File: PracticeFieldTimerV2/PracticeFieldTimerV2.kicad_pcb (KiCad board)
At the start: 2 copper layers, 106 x 153.7 mm, 41 parts, among them J1 External Controls, J3 Panel, J5 /CAN Enable, J6 RJ45-B, J7 RJ45-A, J8 CAN Terminate, U1 ESP32-DevKitC, U2 PCF8574N, U3 20 x 4 LCD, U4 DS3231MZ_TRL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

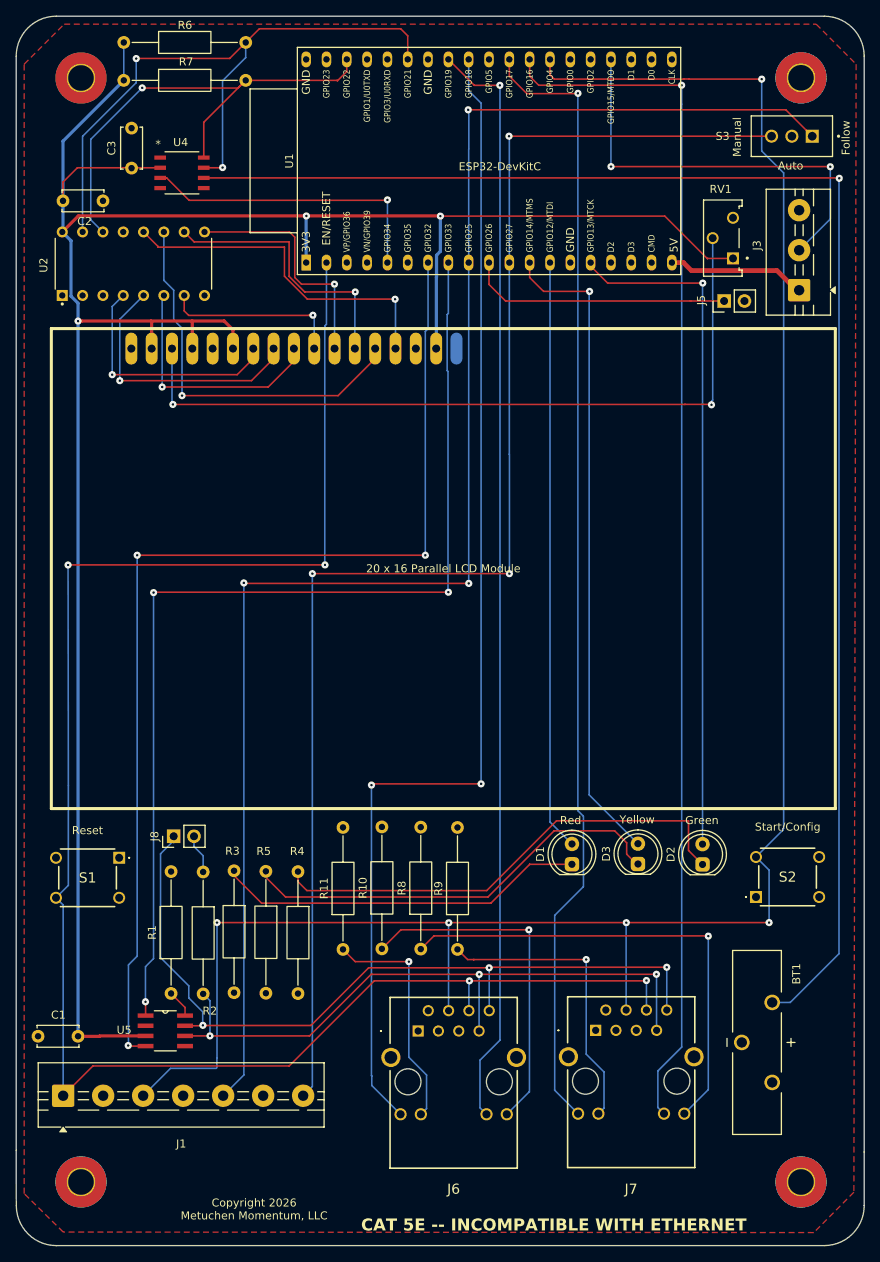
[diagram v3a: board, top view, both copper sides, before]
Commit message: Mark resistors with values. Add mounting holes for the LCD display. Needlessy tweak board width.
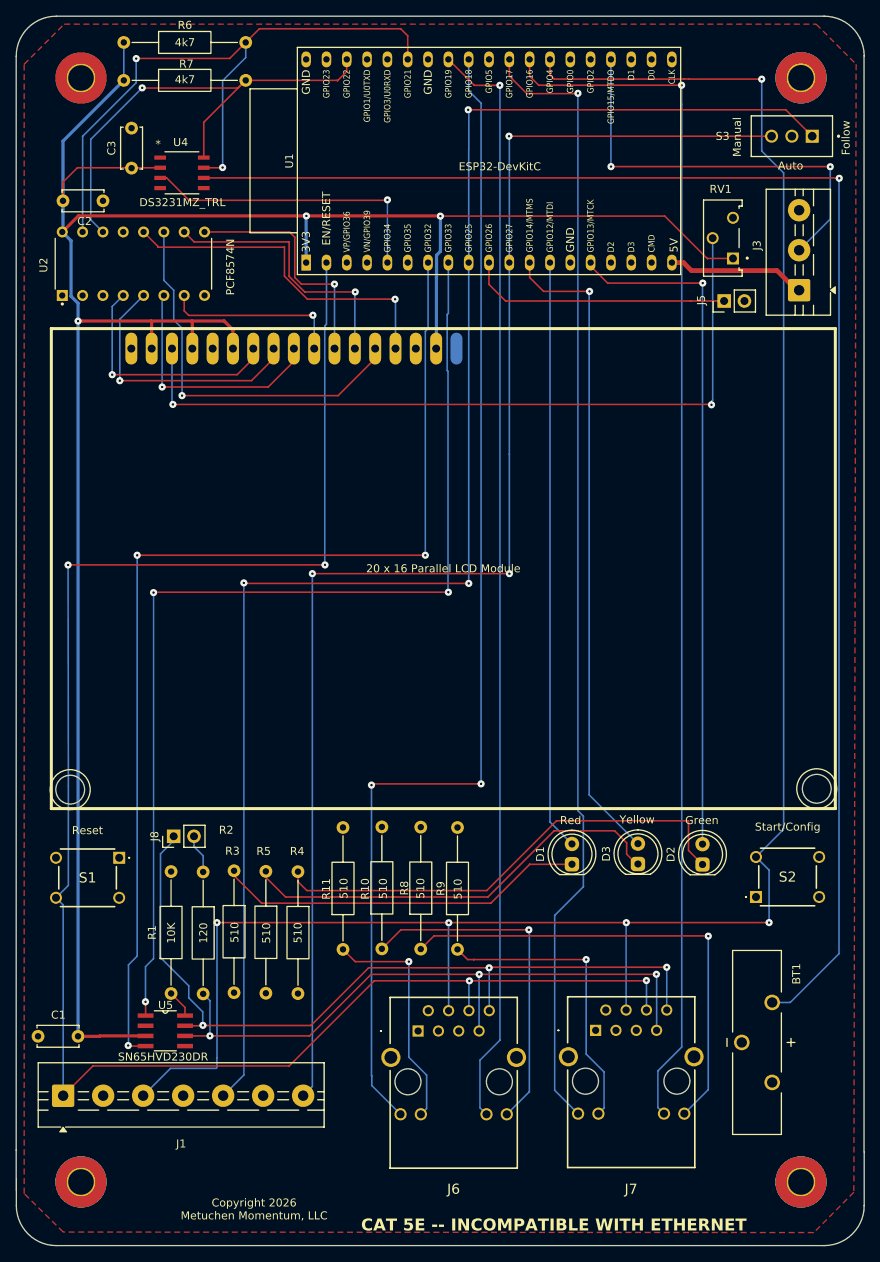
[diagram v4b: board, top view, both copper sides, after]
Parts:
- added REF**: M3_2.5mm_Offset, Misc:M3_HoleWith2.5mmRing, F.Cu at (140.1, 119.6)
- added REF**: M3_2.5mm_Offset, Misc:M3_HoleWith2.5mmRing, F.Cu at (46.8, 119.7)
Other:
- outline, holes or cut-outs redrawn
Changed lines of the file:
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@@
 		(allow_soldermask_bridges_in_footprints no)
 		(tenting front back)
+		(aux_axis_origin 40.01 23.03)
 		(pcbplotparams
 			(layerselection 0x00000000_00000000_55555555_5755f5ff)
@@
 		(embedded_fonts no)
 	)
+	(footprint "Misc:M3_HoleWith2.5mmRing"
+		(layer "F.Cu")
+		(at 140.07 119.57)
+		(property "Reference" "REF**"
+			(at 0 -3.6 0)
+			(unlocked yes)
+			(layer "F.SilkS")
+			(hide yes)
+			(effects
+				(font
+					(size 1 1)
+					(thickness 0.1)
+				)
+			)
+		)
+		(property "Value" "M3_2.5mm_Offset"
+			(at 0 4.2 0)
+			(unlocked yes)
+			(layer "F.Fab")
+			(effects
+				(font
+					(size 1 1)
+					(thickness 0.15)
+				)
+			)
+		)
+		(property "Datasheet" ""
+			(at 0 0 0)
+			(unlocked yes)
+			(layer "F.Fab")
+			(hide yes)
+			(effects
+				(font
+					(size 1 1)
+					(thickness 0.15)
+				)
+			)
+		)
+		(property "Description" "M3 Mounting Hole With 2.5 mm Ring"
+			(at 0 0 0)
+			(unlocked yes)
+			(layer "F.Fab")
+			(hide yes)
+			(effects
+				(font
+					(size 1 1)
+					(thickness 0.15)
+				)
+			)
+		)
+		(attr through_hole)
+		(fp_circle
+			(center 0 0)
+			(end 2.5 0)
+			(stroke
+				(width 0.1)
+				(type solid)
+			)
+			(fill no)
+			(layer "F.SilkS")
+		)
+		(fp_circle
+			(center 0 0)
+			(end 1.8 0)
+			(stroke
+				(width 0.05)
+				(type solid)
+			)
+			(fill no)
+			(layer "Edge.Cuts")
+		)
+		(embedded_fonts no)
+	)
 	(footprint "Misc:SW_500ASSP1M2QE"
 		(locked yes)
@@
 		(tags "Resistor Axial_DIN0207 series Axial Horizontal pin pitch 15.24mm 0.25W = 1/4W length 6.3mm diameter 2.5mm")
 		(property "Reference" "R7"
-			(at 7.79 -2.33 0)
+			(at 7.82 -2.05 0)
 			(layer "F.SilkS")
 			(effects
@@
 		)
 		(property "Value" "4k7"
-			(at 7.62 2.37 0)
-			(layer "F.Fab")
+			(at 7.64 -0.1 0)
+			(layer "F.SilkS")
 			(effects
 				(font
@@
 		(tags "Resistor Axial_DIN0207 series Axial Horizontal pin pitch 15.24mm 0.25W = 1/4W length 6.3mm diameter 2.5mm")
 		(property "Reference" "R5"
-			(at -2.51 0.28 180)
+			(at -2.51 0.28 0)
 			(layer "F.SilkS")
 			(effects
@@
 		)
 		(property "Value" "510"
-			(at 7.62 2.37 90)
-			(layer "F.Fab")
+			(at 7.71 -0.07 90)
+			(layer "F.SilkS")
 			(effects
 				(font
@@
 		(tags "Resistor Axial_DIN0207 series Axial Horizontal pin pitch 15.24mm 0.25W = 1/4W length 6.3mm diameter 2.5mm")
 		(property "Reference" "R4"
-			(at -2.55 0.1 180)
+			(at -2.55 0.1 0)
 			(layer "F.SilkS")
 			(effects
@@
 		)
 		(property "Value" "510"
-			(at 7.62 2.37 90)
-			(layer "F.Fab")
+			(at 7.64 0.01 90)
+			(layer "F.SilkS")
 			(effects
 				(font
@@
 		)
 		(property "Value" "DS3231MZ_TRL"
-			(at 0 -8 0)
+			(at 0.06 3.7 0)
 			(unlocked yes)
-			(layer "F.Fab")
+			(layer "F.SilkS")
 			(effects
 				(font
@@
 		(tags "SN65HVD230DR ")
 		(property "Reference" "U5"
-			(at -5.15 -0.1 0)
+			(at 0.03 -3.21 0)
 			(unlocked yes)
 			(layer "F.SilkS")
@@
 		)
 		(property "Value" "SN65HVD230DR"
-			(at 0 0 0)
+			(at -0.28 3.25 0)
 			(unlocked yes)
-			(layer "F.Fab")
+			(layer "F.SilkS")
 			(effects
 				(font
@@
 		(tags "Resistor Axial_DIN0207 series Axial Horizontal pin pitch 15.24mm 0.25W = 1/4W length 6.3mm diameter 2.5mm")
 		(property "Reference" "R3"
-			(at -2.47 0.2 180)
+			(at -2.47 0.2 0)
 			(layer "F.SilkS")
 			(effects
@@
 		)
 		(property "Value" "510"
-			(at 7.62 2.37 90)
-			(layer "F.Fab")
+			(at 7.7 -0.08 90)
+			(layer "F.SilkS")
 			(effects
 				(font
@@
 		)
 		(property "Value" "PCF8574N"
-			(at 11.275 10.835 90)
-			(layer "F.Fab")
+			(at -0.41 12.13 90)
+			(layer "F.SilkS")
 			(effects
 				(font
@@
 		(tags "Resistor Axial_DIN0207 series Axial Horizontal pin pitch 15.24mm 0.25W = 1/4W length 6.3mm diameter 2.5mm")
 		(property "Reference" "R8"
-			(at 7.62 -2.37 90)
+			(at 7.62 -2.04 90)
 			(layer "F.SilkS")
 			(effects
@@
 		)
 		(property "Value" "510"
-			(at 7.62 2.37 90)
-			(layer "F.Fab")
+			(at 7.58 -0.02 90)
+			(layer "F.SilkS")
 			(effects
 				(font
@@
 		(tags "Resistor Axial_DIN0207 series Axial Horizontal pin pitch 15.24mm 0.25W = 1/4W length 6.3mm diameter 2.5mm")
 		(property "Reference" "R11"
-			(at 7.62 -2.37 90)
+			(at 7.55 -2.09 90)
 			(layer "F.SilkS")
 			(effects
@@
 		)
 		(property "Value" "510"
-			(at 7.62 2.37 90)
-			(layer "F.Fab")
+			(at 7.62 0.1 90)
+			(layer "F.SilkS")
 			(effects
 				(font
@@
 		(tags "Resistor Axial_DIN0207 series Axial Horizontal pin pitch 15.24mm 0.25W = 1/4W length 6.3mm diameter 2.5mm")
 		(property "Reference" "R9"
-			(at 7.62 -2.37 90)
+			(at 7.61 -2.09 90)
 			(layer "F.SilkS")
 			(effects
@@
 		)
 		(property "Value" "510"
-			(at 7.62 2.37 90)
-			(layer "F.Fab")
+			(at 7.54 0.06 90)
+			(layer "F.SilkS")
 			(effects
 				(font
@@
 		)
 	)
+	(footprint "Misc:M3_HoleWith2.5mmRing"
+		(layer "F.Cu")
+		(at 46.75 119.68)
+		(property "Reference" "REF**"
+			(at 0 -3.6 0)
+			(unlocked yes)
+			(layer "F.SilkS")
+			(hide yes)
+			(effects
+				(font
+					(size 1 1)
+					(thickness 0.1)
+				)
+			)
+		)
+		(property "Value" "M3_2.5mm_Offset"
+			(at 0 4.2 0)
+			(unlocked yes)
+			(layer "F.Fab")
+			(effects
+				(font
+					(size 1 1)
+					(thickness 0.15)
+				)
+			)
+		)
+		(property "Datasheet" ""
+			(at 0 0 0)
+			(unlocked yes)
+			(layer "F.Fab")
+			(hide yes)
+			(effects
+				(font
+					(size 1 1)
+					(thickness 0.15)
+				)
+			)
+		)
+		(property "Description" "M3 Mounting Hole With 2.5 mm Ring"
+			(at 0 0 0)
+			(unlocked yes)
+			(layer "F.Fab")
+			(hide yes)
+			(effects
+				(font
+					(size 1 1)
+					(thickness 0.15)
+				)
+			)
+		)
+		(attr through_hole)
+		(fp_circle
+			(center 0 0)
+			(end 2.5 0)
+			(stroke
+				(width 0.1)
+				(type solid)
+			)
+			(fill no)
+			(layer "F.SilkS")
+		)
+		(fp_circle
+			(center 0 0)
+			(end 1.8 0)
+			(stroke
+				(width 0.05)
+				(type solid)
+			)
+			(fill no)
+			(layer "Edge.Cuts")
+		)
+		(embedded_fonts no)
+	)
 	(footprint "Resistor_THT:R_Axial_DIN0207_L6.3mm_D2.5mm_P15.24mm_Horizontal"
 		(layer "F.Cu")
@@
 		(tags "Resistor Axial_DIN0207 series Axial Horizontal pin pitch 15.24mm 0.25W = 1/4W length 6.3mm diameter 2.5mm")
 		(property "Reference" "R10"
-			(at 7.62 -2.37 90)
+			(at 7.49 -2.09 90)
 			(layer "F.SilkS")
 			(effects
@@
 		)
 		(property "Value" "510"
-			(at 7.62 2.37 90)
-			(layer "F.Fab")
+			(at 7.53 0.16 90)
+			(layer "F.SilkS")
 			(effects
 				(font
@@
 		)
 		(property "Value" "4k7"
-			(at 7.62 2.37 0)
-			(layer "F.Fab")
+			(at 7.64 0.01 0)
+			(layer "F.SilkS")
 			(effects
 				(font
@@
 		(tags "Resistor Axial_DIN0207 series Axial Horizontal pin pitch 15.24mm 0.25W = 1/4W length 6.3mm diameter 2.5mm")
 		(property "Reference" "R2"
-			(at 17.37 -0.83 180)
+			(at -5.24 -2.88 0)
 			(layer "F.SilkS")
 			(effects
@@
 		)
 		(property "Value" "120"
-			(at 7.62 2.37 90)
-			(layer "F.Fab")
+			(at 7.63 -0.04 90)
+			(layer "F.SilkS")
 			(effects
 				(font
@@
 		)
 		(property "Value" "10K"
-			(at 7.62 2.37 90)
-			(layer "F.Fab")
+			(at 7.56 0.03 90)
+			(layer "F.SilkS")
 			(effects
 				(font
@@
 	)
 	(gr_line
-		(start 146 28)
-		(end 146 164.975)
+		(start 145.98 27.96)
+		(end 145.98 164.935)
 		(stroke
 			(width 0.05)
@@
 		(layer "Edge.Cuts")
 	)
+	(gr_arc
+		(start 145.423515 25.669224)
+		(mid 145.848874 26.77999)
+		(end 145.999838 27.959796)
+		(stroke
+			(width 0.05)
+			(type default)
+		)
+		(layer "Edge.Cuts")
+	)
 	(gr_line
 		(start 45 23)
@@
 	(gr_arc
 		(start 141 23)
-		(mid 144.535534 24.464466)
-		(end 146 28)
+		(mid 143.583227 23.719002)
+		(end 145.423515 25.669224)
 		(stroke
 			(width 0.05)
@@
 		(layer "Edge.Cuts")
 	)
+	(gr_line
+		(start 65.97 125.56)
+		(end 64.31 128.87)
+		(stroke
+			(width 0.1)
+			(type default)
+		)
+		(layer "User.3")
+	)
 	(gr_text "Reset"

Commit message: Fix traces broken in the previous commit.
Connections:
- BT1 pad P_2: Net-(U4-VBAT) -> (no net)
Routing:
- net GND: track 0.00 -> 32.2 mm, vias 0 -> 2
- net /RST: track 224.6 -> 231.1 mm
- net +3.3V: track 293.7 -> 298.6 mm
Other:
- outline, holes or cut-outs redrawn
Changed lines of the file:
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@@
 			(layers "*.Cu" "*.Mask")
 			(remove_unused_layers no)
-			(net 63 "Net-(U4-VBAT)")
 			(pintype "passive")
 			(solder_mask_margin 0.102)
@@
 	)
 	(gr_line
-		(start 146 164.975)
+		(start 141 23)
+		(end 145.97 23)
+		(stroke
+			(width 0.05)
+			(type default)
+		)
+		(layer "Edge.Cuts")
+	)
+	(gr_line
+		(start 145.98 164.935)
 		(end 146 171.675)
 		(stroke
@@
 		(layer "Edge.Cuts")
 	)
-	(gr_arc
-		(start 145.423515 25.669224)
-		(mid 145.848874 26.77999)
-		(end 145.999838 27.959796)
+	(gr_line
+		(start 140.56 23)
+		(end 141 23)
 		(stroke
 			(width 0.05)
@@
 	(gr_line
 		(start 45 23)
-		(end 141 23)
+		(end 140.56 23)
 		(stroke
 			(width 0.05)
@@
 		(layer "Edge.Cuts")
 	)
-	(gr_arc
-		(start 141 23)
-		(mid 143.583227 23.719002)
-		(end 145.423515 25.669224)
+	(gr_line
+		(start 40 164.75)
+		(end 40 28)
 		(stroke
 			(width 0.05)
@@
 	)
 	(gr_line
-		(start 40 164.75)
-		(end 40 28)
+		(start 145.97 23)
+		(end 145.98 27.96)
 		(stroke
 			(width 0.05)
-			(type default)
+			(type solid)
 		)
 		(layer "Edge.Cuts")
@@
 	)
 	(segment
+		(start 47.73 113.95)
+		(end 47.73 58.882907)
+		(width 0.4)
+		(layer "B.Cu")
+		(net 1)
+	)
+	(segment
+		(start 49.52 124.65)
+		(end 47.94 124.65)
+		(width 0.4)
+		(layer "B.Cu")
+		(net 1)
+	)
+	(segment
 		(start 56.932088 64.547963)
 		(end 56.7 64.315875)
@@
 	)
 	(segment
-		(start 47.73 150.51)
-		(end 47.73 58.882907)
+		(start 51.22 122.95)
+		(end 49.52 124.65)
 		(width 0.4)
 		(layer "B.Cu")
@@
 	)
 	(segment
+		(start 49.35 113.95)
+		(end 51.38 115.98)
+		(width 0.4)
+		(layer "B.Cu")
+		(net 1)
+	)
+	(segment
 		(start 76.242088 47.997912)
 		(end 76.27 47.97)
@@
 	)
 	(segment
+		(start 47.73 113.95)
+		(end 49.35 113.95)
+		(width 0.4)
+		(layer "B.Cu")
+		(net 1)
+	)
+	(segment
 		(start 53.45 31.02)
 		(end 53.45 26.28)
@@
 	)
 	(segment
+		(start 47.73 124.86)
+		(end 47.94 124.65)
+		(width 0.4)
+		(layer "B.Cu")
+		(net 1)
+	)
+	(segment
 		(start 92.522928 55.617123)
 		(end 92.522928 63.297383)
@@
 	)
 	(segment
+		(start 47.73 150.51)
+		(end 47.73 124.86)
+		(width 0.4)
+		(layer "B.Cu")
+		(net 1)
+	)
+	(segment
+		(start 51.38 115.98)
+		(end 51.38 122.79)
+		(width 0.4)
+		(layer "B.Cu")
+		(net 1)
+	)
+	(segment
+		(start 51.38 122.79)
+		(end 51.22 122.95)
+		(width 0.4)
+		(layer "B.Cu")
+		(net 1)
+	)
+	(segment
+		(start 63.54 57.89)
+		(end 62.32 56.67)
+		(width 0.2)
+		(layer "F.Cu")
+		(net 2)
+	)
+	(segment
+		(start 50.88 57.91)
+		(end 50.84 57.91)
+		(width 0.2)
+		(layer "F.Cu")
+		(net 2)
+	)
+	(segment
+		(start 64.552088 66.017912)
+		(end 63.62 66.95)
+		(width 0.2)
+		(layer "F.Cu")
+		(net 2)
+	)
+	(segment
+		(start 54.392088 65.797643)
+		(end 54.392088 64.547963)
+		(width 0.2)
+		(layer "F.Cu")
+		(net 2)
+	)
+	(segment
+		(start 63.54 57.91)
+		(end 63.54 57.89)
+		(width 0.2)
+		(layer "F.Cu")
+		(net 2)
+	)
+	(segment
+		(start 62.32 56.67)
+		(end 52.12 56.67)
+		(width 0.2)
+		(layer "F.Cu")
+		(net 2)
+	)
+	(segment
+		(start 64.552088 64.547963)
+		(end 64.552088 66.017912)
+		(width 0.2)
+		(layer "F.Cu")
+		(net 2)
+	)
+	(segment
+		(start 63.62 66.95)
+		(end 55.544445 66.95)
+		(width 0.2)
+		(layer "F.Cu")
+		(net 2)
+	)
+	(segment
+		(start 55.544445 66.95)
+		(end 54.392088 65.797643)
+		(width 0.2)
+		(layer "F.Cu")
+		(net 2)
+	)
+	(segment
+		(start 52.12 56.67)
+		(end 50.88 57.91)
+		(width 0.2)
+		(layer "F.Cu")
+		(net 2)
+	)
+	(via
+		(at 75.86 68.86)
+		(size 0.9)
+		(drill 0.3)
+		(layers "F.Cu" "B.Cu")
+		(free yes)
+		(net 2)
+	)
+	(via
+		(at 75.9 73.54)
+		(size 0.9)
+		(drill 0.3)
+		(layers "F.Cu" "B.Cu")
+		(free yes)
+		(net 2)
+	)
+	(segment
+		(start 75.9 68.9)
+		(end 75.86 68.86)
+		(width 0.2)
+		(layer "B.Cu")
+		(net 2)
+	)
+	(segment
+		(start 75.9 73.54)
+		(end 75.9 68.9)
+		(width 0.2)
+		(layer "B.Cu")
+		(net 2)
+	)
+	(segment
+		(start 75.86 73.5)
+		(end 75.9 73.54)
+		(width 0.2)
+		(layer "B.Cu")
+		(net 2)
+	)
+	(segment
 		(start 66.82 130.02)
 		(end 70.67 133.87)
@@
 	)
 	(segment
-		(start 44.972088 133.197963)
-		(end 45.87 134.095875)
+		(start 49.19 114.95)
+		(end 50.65 116.41)
 		(width 0.2)
 		(layer "B.Cu")
@@
 	)
 	(segment
-		(start 46.522088 119.197963)
-		(end 46.522088 131.647963)
+		(start 44.972088 133.197963)
+		(end 45.87 134.095875)
 		(width 0.2)
 		(layer "B.Cu")
@@
 	)
 	(segment
-		(start 46.522088 131.647963)
-		(end 44.972088 133.197963)
+		(start 46.522088 123.95)
+		(end 46.522088 131.647963)
 		(width 0.2)
 		(layer "B.Cu")
@@
 	)
 	(segment
+		(start 46.522088 131.647963)
+		(end 44.972088 133.197963)
+		(width 0.2)
+		(layer "B.Cu")
+		(net 12)
+	)
+	(segment
+		(start 46.515923 114.95)
+		(end 49.19 114.95)
+		(width 0.2)
+		(layer "B.Cu")
+		(net 12)
+	)
+	(segment
+		(start 46.482033 91.6)
+		(end 46.515923 114.95)
+		(width 0.2)
+		(layer "B.Cu")
+		(net 12)
+	)
+	(segment
 		(start 44.972088 133.197963)
 		(end 44.972088 133.702088)
@@
 	)
 	(segment
-		(start 96.59 147.31)
-		(end 96.59 143.64)
+		(start 49.11 123.95)
+		(end 46.522088 123.95)
 		(width 0.2)
 		(layer "B.Cu")
@@
 	)
 	(segment
-		(start 46.482033 91.6)
-		(end 46.522088 119.197963)
+		(start 96.59 147.31)
+		(end 96.59 143.64)
 		(width 0.2)
 		(layer "B.Cu")
@@
 		(width 0.2)
 		(layer "B.Cu")
+		(net 12)
+	)
+	(segment
+		(start 50.65 122.41)
+		(end 49.11 123.95)
+		(width 0.2)
+		(layer "B.Cu")
+		(net 12)
+	)
+	(segment
+		(start 50.65 116.41)
+		(end 50.65 122.41)
+		(width 0.2)
+		(layer "B.Cu")
